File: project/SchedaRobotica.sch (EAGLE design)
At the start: 105 parts, among them IC1 LMZ14202TZE-ADJ_NOPB, IC2 VNH7070ASTR, IC3 VNH7070ASTR, IC4 VNH7070ASTR, IC5 VNH7070ASTR, M1 43650-0201, M2 43650-0201, M3 43650-0201, M4 43650-0201

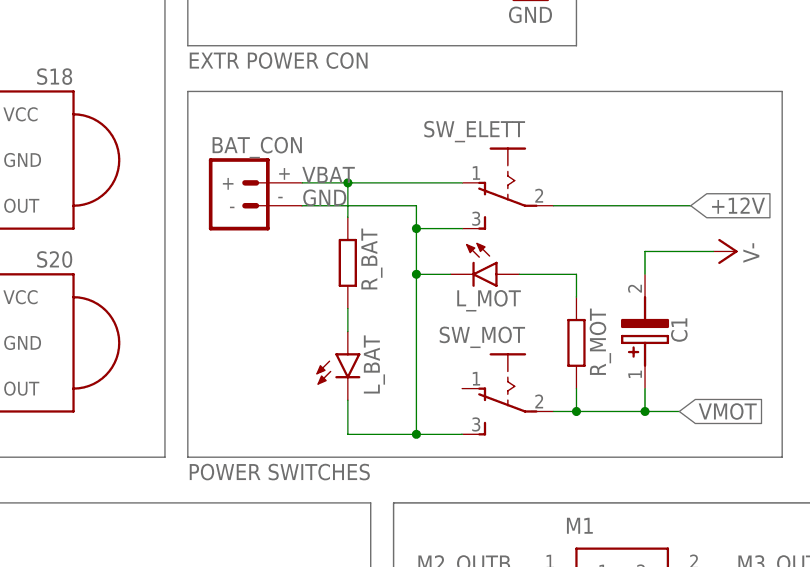
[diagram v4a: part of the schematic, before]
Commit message: started placing components for optimal wiring
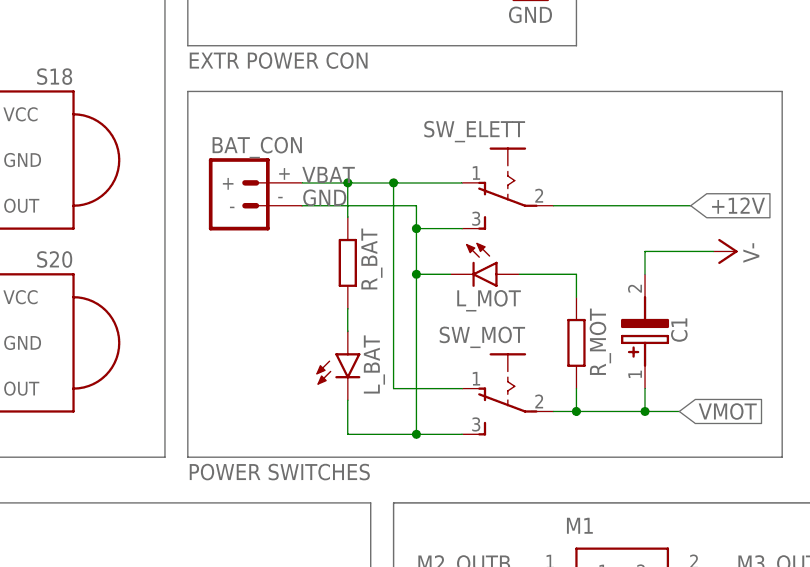
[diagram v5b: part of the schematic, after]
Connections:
- net VBAT: now also SW_MOT.O
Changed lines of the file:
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@@
 <grid distance="0.1" unitdist="inch" unit="inch" style="lines" multiple="1" display="no" altdistance="0.01" altunitdist="inch" altunit="inch"/>
 <layers>
-<layer number="1" name="Top" color="4" fill="1" visible="no" active="no"/>
-<layer number="16" name="Bottom" color="1" fill="1" visible="no" active="no"/>
-<layer number="17" name="Pads" color="2" fill="1" visible="no" active="no"/>
-<layer number="18" name="Vias" color="2" fill="1" visible="no" active="no"/>
-<layer number="19" name="Unrouted" color="6" fill="1" visible="no" active="no"/>
-<layer number="20" name="Dimension" color="24" fill="1" visible="no" active="no"/>
-<layer number="21" name="tPlace" color="7" fill="1" visible="no" active="no"/>
-<layer number="22" name="bPlace" color="7" fill="1" visible="no" active="no"/>
-<layer number="23" name="tOrigins" color="15" fill="1" visible="no" active="no"/>
-<layer number="24" name="bOrigins" color="15" fill="1" visible="no" active="no"/>
-<layer number="25" name="tNames" color="7" fill="1" visible="no" active="no"/>
-<layer number="26" name="bNames" color="7" fill="1" visible="no" active="no"/>
-<layer number="27" name="tValues" color="7" fill="1" visible="no" active="no"/>
-<layer number="28" name="bValues" color="7" fill="1" visible="no" active="no"/>
+<layer number="1" name="Top" color="4" fill="1" visible="yes" active="no"/>
+<layer number="16" name="Bottom" color="1" fill="1" visible="yes" active="no"/>
+<layer number="17" name="Pads" color="2" fill="1" visible="yes" active="no"/>
+<layer number="18" name="Vias" color="2" fill="1" visible="yes" active="no"/>
+<layer number="19" name="Unrouted" color="6" fill="1" visible="yes" active="no"/>
+<layer number="20" name="Dimension" color="24" fill="1" visible="yes" active="no"/>
+<layer number="21" name="tPlace" color="7" fill="1" visible="yes" active="no"/>
+<layer number="22" name="bPlace" color="7" fill="1" visible="yes" active="no"/>
+<layer number="23" name="tOrigins" color="15" fill="1" visible="yes" active="no"/>
+<layer number="24" name="bOrigins" color="15" fill="1" visible="yes" active="no"/>
+<layer number="25" name="tNames" color="7" fill="1" visible="yes" active="no"/>
+<layer number="26" name="bNames" color="7" fill="1" visible="yes" active="no"/>
+<layer number="27" name="tValues" color="7" fill="1" visible="yes" active="no"/>
+<layer number="28" name="bValues" color="7" fill="1" visible="yes" active="no"/>
 <layer number="29" name="tStop" color="7" fill="3" visible="no" active="no"/>
 <layer number="30" name="bStop" color="7" fill="6" visible="no" active="no"/>
@@
 <layer number="35" name="tGlue" color="7" fill="4" visible="no" active="no"/>
 <layer number="36" name="bGlue" color="7" fill="5" visible="no" active="no"/>
-<layer number="37" name="tTest" color="7" fill="1" visible="no" active="no"/>
-<layer number="38" name="bTest" color="7" fill="1" visible="no" active="no"/>
+<layer number="37" name="tTest" color="7" fill="1" visible="yes" active="no"/>
+<layer number="38" name="bTest" color="7" fill="1" visible="yes" active="no"/>
 <layer number="39" name="tKeepout" color="4" fill="11" visible="no" active="no"/>
 <layer number="40" name="bKeepout" color="1" fill="11" visible="no" active="no"/>
@@
 <layer number="44" name="Drills" color="7" fill="1" visible="no" active="no"/>
 <layer number="45" name="Holes" color="7" fill="1" visible="no" active="no"/>
-<layer number="46" name="Milling" color="3" fill="1" visible="no" active="no"/>
-<layer number="47" name="Measures" color="7" fill="1" visible="no" active="no"/>
-<layer number="48" name="Document" color="7" fill="1" visible="no" active="no"/>
-<layer number="49" name="Reference" color="7" fill="1" visible="no" active="no"/>
-<layer number="50" name="dxf" color="7" fill="1" visible="no" active="no"/>
-<layer number="51" name="tDocu" color="7" fill="1" visible="no" active="no"/>
-<layer number="52" name="bDocu" color="7" fill="1" visible="no" active="no"/>
-<layer number="53" name="tGND_GNDA" color="7" fill="9" visible="no" active="no"/>
-<layer number="54" name="bGND_GNDA" color="1" fill="9" visible="no" active="no"/>
-<layer number="56" name="wert" color="7" fill="1" visible="no" active="no"/>
-<layer number="57" name="tCAD" color="7" fill="1" visible="no" active="no"/>
-<layer number="59" name="tCarbon" color="7" fill="1" visible="no" active="no"/>
-<layer number="60" name="bCarbon" color="7" fill="1" visible="no" active="no"/>
-<layer number="61" name="stand" color="7" fill="1" visible="no" active="no"/>
+<layer number="46" name="Milling" color="3" fill="1" visible="yes" active="no"/>
+<layer number="47" name="Measures" color="7" fill="1" visible="yes" active="no"/>
+<layer number="48" name="Document" color="7" fill="1" visible="yes" active="no"/>
+<layer number="49" name="Reference" color="7" fill="1" visible="yes" active="no"/>
+<layer number="50" name="dxf" color="7" fill="1" visible="yes" active="no"/>
+<layer number="51" name="tDocu" color="7" fill="1" visible="yes" active="no"/>
+<layer number="52" name="bDocu" color="7" fill="1" visible="yes" active="no"/>
+<layer number="53" name="tGND_GNDA" color="7" fill="9" visible="yes" active="no"/>
+<layer number="54" name="bGND_GNDA" color="1" fill="9" visible="yes" active="no"/>
+<layer number="56" name="wert" color="7" fill="1" visible="yes" active="no"/>
+<layer number="57" name="tCAD" color="7" fill="1" visible="yes" active="no"/>
+<layer number="59" name="tCarbon" color="7" fill="1" visible="yes" active="no"/>
+<layer number="60" name="bCarbon" color="7" fill="1" visible="yes" active="no"/>
+<layer number="61" name="stand" color="7" fill="1" visible="yes" active="no"/>
 <layer number="88" name="SimResults" color="9" fill="1" visible="yes" active="yes"/>
 <layer number="89" name="SimProbes" color="9" fill="1" visible="yes" active="yes"/>
@@
 <wire x1="248.92" y1="223.52" x2="254" y2="223.52" width="0.1524" layer="91"/>
 <pinref part="R_BAT" gate="G$1" pin="1"/>
-<wire x1="254" y1="223.52" x2="266.7" y2="223.52" width="0.1524" layer="91"/>
+<wire x1="254" y1="223.52" x2="259.08" y2="223.52" width="0.1524" layer="91"/>
+<wire x1="259.08" y1="223.52" x2="266.7" y2="223.52" width="0.1524" layer="91"/>
 <wire x1="254" y1="219.71" x2="254" y2="223.52" width="0.1524" layer="91"/>
 <junction x="254" y="223.52"/>
 <label x="248.92" y="223.52" size="1.778" layer="95"/>
-</segment>
-</net>
+<pinref part="SW_MOT" gate="1" pin="O"/>
+<wire x1="266.7" y1="200.66" x2="259.08" y2="200.66" width="0.1524" layer="91"/>
+<wire x1="259.08" y1="200.66" x2="259.08" y2="223.52" width="0.1524" layer="91"/>
+<junction x="259.08" y="223.52"/>
+</segment>
+</net>

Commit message: added IMU and BT
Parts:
- added BT_CON: 4P-2.0, OPL_Connector:GROVE-CONNECTOR-DIP(4P-2.0)
- added C19, C20: 1u, rcl:C-EUC0805
- added R21, R22: 10k, rcl:R-EU_M0805
- added U$3: (no value), BNO055ada:BNO055
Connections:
- new net IFE: BT_CON.3
- new net N$39: BT_CON.4
- new net SCL: R21.1, U$3.SCL
- new net SDA: R22.1, U$3.SDA
- net +3V3: now also BT_CON.1, C19.1, C20.1, R21.2, R22.2, U$3.3V3
- net GND: now also BT_CON.2, C19.2, C20.2, U$3.GND
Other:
- note added: "BLUETOOTH"
- note added: "IMU"
- note added: "TODO: -add BT serial -add roller and kicker connectors (?)"
- note removed: "TODO: -add BT connector (Grove) -add roller and kicker connectors (?)"

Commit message: added ball switches, what now?
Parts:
- added B_SW_1, B_SW_2: 21810LPSTF, 21810LPSTF:21810LPSTF
- added SV5: (no value), con-lstb:MA12-1
- added SV6: (no value), SparkFun-Connectors:CONN_14LONGPADS
- U$3: value (none) -> BNO055_BNO055; device BNO055ada:BNO055 -> IMU:BNO055_BNO055
- renumbered R4 to R_ELETT
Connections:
- net GND: now also U$1.GND1, U$1.GND2, U$1.GND3, U$1.GND4, U$1.GND5, U$1.GND6
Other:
- note added: "BALL SWITCHES"
- note added: "TODO: -add serials and values -add roller and kicker connectors (?) -add US cons if there's room"
- note removed: "TODO: -add BT serial -add roller and kicker connectors (?)"
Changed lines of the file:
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@@
 <layer number="195" name="mNames" color="7" fill="1" visible="no" active="yes"/>
 <layer number="196" name="mValues" color="7" fill="1" visible="no" active="yes"/>
+<layer number="197" name="ARDUINO_b_PLACE" color="7" fill="1" visible="yes" active="yes"/>
 <layer number="199" name="Contour" color="7" fill="1" visible="no" active="yes"/>
 <layer number="200" name="200bmp" color="1" fill="10" visible="yes" active="yes"/>
@@
 <part name="R2" library="rcl" library_urn="urn:adsk.eagle:library:334" deviceset="R-EU_" device="M0805" package3d_urn="urn:adsk.eagle:package:23556/2"/>
 <part name="R3" library="rcl" library_urn="urn:adsk.eagle:library:334" deviceset="R-EU_" device="M0805" package3d_urn="urn:adsk.eagle:package:23556/2"/>
-<part name="R4" library="rcl" library_urn="urn:adsk.eagle:library:334" deviceset="R-EU_" device="M0805" package3d_urn="urn:adsk.eagle:package:23556/2"/>
+<part name="R_ELETT" library="rcl" library_urn="urn:adsk.eagle:library:334" deviceset="R-EU_" device="M0805" package3d_urn="urn:adsk.eagle:package:23556/2"/>
 <part name="+3V6" library="supply1" library_urn="urn:adsk.eagle:library:371" deviceset="+3V3" device=""/>
 <part name="GND27" library="supply1" library_urn="urn:adsk.eagle:library:371" deviceset="GND" device=""/>
@@
 <part name="M4-" library="led" library_urn="urn:adsk.eagle:library:259" deviceset="LED" device="CHIPLED_1206" package3d_urn="urn:adsk.eagle:package:15823/2"/>
 <part name="M4+" library="led" library_urn="urn:adsk.eagle:library:259" deviceset="LED" device="CHIPLED_1206" package3d_urn="urn:adsk.eagle:package:15823/2"/>
-<part name="U$3" library="BNO055ada" deviceset="BNO055" device=""/>
+<part name="U$3" library="IMU" deviceset="BNO055_BNO055" device=""/>
 <part name="C19" library="rcl" library_urn="urn:adsk.eagle:library:334" deviceset="C-EU" device="C0805" package3d_urn="urn:adsk.eagle:package:23617/2" value="1u"/>
 <part name="R21" library="rcl" library_urn="urn:adsk.eagle:library:334" deviceset="R-EU_" device="M0805" package3d_urn="urn:adsk.eagle:package:23556/2" value="10k"/>
@@
 <part name="+3V14" library="supply1" library_urn="urn:adsk.eagle:library:371" deviceset="+3V3" device=""/>
 <part name="GND39" library="supply1" library_urn="urn:adsk.eagle:library:371" deviceset="GND" device=""/>
+<part name="GND40" library="supply1" library_urn="urn:adsk.eagle:library:371" deviceset="GND" device=""/>
+<part name="SV5" library="con-lstb" library_urn="urn:adsk.eagle:library:162" deviceset="MA12-1" device="" package3d_urn="urn:adsk.eagle:package:8348/1"/>
+<part name="SV6" library="SparkFun-Connectors" deviceset="CONN_14" device="LONGPADS"/>
+<part name="B_SW_1" library="21810LPSTF" deviceset="21810LPSTF" device=""/>
+<part name="B_SW_2" library="21810LPSTF" deviceset="21810LPSTF" device=""/>
 </parts>
 <sheets>
@@
 <text x="259.08" y="142.24" size="1.778" layer="97">MOTOR CONS</text>
 <text x="281.94" y="248.92" size="1.778" layer="91">TODO:
--add BT serial
--add roller and kicker connectors (?)</text>
+-add serials and values
+-add roller and kicker connectors (?)
+-add US cons if there's room</text>
 <text x="340.36" y="101.6" size="2.54" layer="97">M1</text>
 <text x="449.58" y="101.6" size="2.54" layer="97">M2</text>
@@
 <text x="449.58" y="44.45" size="2.54" layer="97">M4</text>
 <wire x1="312.42" y1="187.96" x2="312.42" y2="139.7" width="0.1524" layer="97"/>
-<wire x1="312.42" y1="139.7" x2="363.22" y2="139.7" width="0.1524" layer="97"/>
-<wire x1="363.22" y1="139.7" x2="363.22" y2="187.96" width="0.1524" layer="97"/>
-<wire x1="363.22" y1="187.96" x2="312.42" y2="187.96" width="0.1524" layer="97"/>
+<wire x1="312.42" y1="139.7" x2="365.76" y2="139.7" width="0.1524" layer="97"/>
+<wire x1="365.76" y1="139.7" x2="365.76" y2="187.96" width="0.1524" layer="97"/>
+<wire x1="365.76" y1="187.96" x2="312.42" y2="187.96" width="0.1524" layer="97"/>
 <text x="312.42" y="137.16" size="1.778" layer="97">IMU</text>
 <wire x1="304.8" y1="233.68" x2="304.8" y2="203.2" width="0.1524" layer="97"/>
@@
 <wire x1="332.74" y1="233.68" x2="304.8" y2="233.68" width="0.1524" layer="97"/>
 <text x="304.8" y="200.66" size="1.778" layer="97">BLUETOOTH</text>
+<wire x1="368.3" y1="187.96" x2="368.3" y2="139.7" width="0.1524" layer="97"/>
+<wire x1="368.3" y1="139.7" x2="457.2" y2="139.7" width="0.1524" layer="97"/>
+<wire x1="457.2" y1="139.7" x2="457.2" y2="187.96" width="0.1524" layer="97"/>
+<wire x1="457.2" y1="187.96" x2="368.3" y2="187.96" width="0.1524" layer="97"/>
+<text x="368.3" y="137.16" size="1.778" layer="97">BALL SWITCHES</text>
 </plain>
 <instances>
-<instance part="U$1" gate="G$1" x="45.72" y="50.8" smashed="yes"/>
+<instance part="U$1" gate="G$1" x="40.64" y="55.88" smashed="yes"/>
 <instance part="SV1" gate="1" x="86.36" y="81.28" smashed="yes" rot="R180">
 <attribute name="VALUE" x="87.63" y="99.06" size="1.778" layer="96" rot="R180"/>
@@
 <attribute name="VALUE" x="252.73" y="49.022" size="1.778" layer="96" rot="R180"/>
 </instance>
-<instance part="R4" gate="G$1" x="278.13" y="44.45" smashed="yes" rot="R90">
+<instance part="R_ELETT" gate="G$1" x="278.13" y="44.45" smashed="yes" rot="R90">
 <attribute name="NAME" x="281.7114" y="40.64" size="1.778" layer="95" rot="R90"/>
 <attribute name="VALUE" x="281.432" y="40.64" size="1.778" layer="96" rot="R90"/>
@@
 <attribute name="VALUE" x="417.195" y="14.478" size="1.778" layer="96" rot="R90"/>
 </instance>
-<instance part="U$3" gate="G$1" x="340.36" y="152.4" smashed="yes" rot="R270"/>
+<instance part="U$3" gate="G$1" x="340.36" y="152.4" smashed="yes"/>
 <instance part="C19" gate="G$1" x="332.74" y="172.72" smashed="yes">
 <attribute name="NAME" x="334.264" y="173.101" size="1.778" layer="95"/>
@@
 <instance part="GND39" gate="1" x="325.12" y="208.28" smashed="yes">
 <attribute name="VALUE" x="322.58" y="205.74" size="1.778" layer="96"/>
+</instance>
+<instance part="GND40" gate="1" x="45.72" y="6.35" smashed="yes">
+<attribute name="VALUE" x="43.18" y="3.81" size="1.778" layer="96"/>
+</instance>
+<instance part="SV5" gate="1" x="121.92" y="78.74" smashed="yes">
+<attribute name="VALUE" x="120.65" y="60.96" size="1.778" layer="96"/>
+<attribute name="NAME" x="120.65" y="97.282" size="1.778" layer="95"/>
+</instance>
+<instance part="SV6" gate="G$1" x="182.88" y="55.88" smashed="yes" rot="R180">
+<attribute name="VALUE" x="182.88" y="78.486" size="1.778" layer="96" font="vector" rot="R180"/>
+<attribute name="NAME" x="182.88" y="37.592" size="1.778" layer="95" font="vector" rot="R180"/>
+</instance>
+<instance part="B_SW_1" gate="G$1" x="386.08" y="172.72" smashed="yes">
+<attribute name="NAME" x="392.43" y="177.8" size="1.778" layer="95" align="center-left"/>
+</instance>
+<instance part="B_SW_2" gate="G$1" x="421.64" y="172.72" smashed="yes">
+<attribute name="NAME" x="427.99" y="177.8" size="1.778" layer="95" align="center-left"/>
 </instance>
 </instances>
@@
 <junction x="325.12" y="212.09"/>
 </segment>
+<segment>
+<pinref part="U$1" gate="G$1" pin="GND1"/>
+<wire x1="33.02" y1="12.7" x2="33.02" y2="10.16" width="0.1524" layer="91"/>
+<wire x1="33.02" y1="10.16" x2="35.56" y2="10.16" width="0.1524" layer="91"/>
+<pinref part="U$1" gate="G$1" pin="GND6"/>
+<wire x1="35.56" y1="10.16" x2="38.1" y2="10.16" width="0.1524" layer="91"/>
+<wire x1="38.1" y1="10.16" x2="40.64" y2="10.16" width="0.1524" layer="91"/>
+<wire x1="40.64" y1="10.16" x2="43.18" y2="10.16" width="0.1524" layer="91"/>
+<wire x1="43.18" y1="10.16" x2="45.72" y2="10.16" width="0.1524" layer="91"/>
+<wire x1="45.72" y1="10.16" x2="45.72" y2="12.7" width="0.1524" layer="91"/>
+<pinref part="U$1" gate="G$1" pin="GND2"/>
+<wire x1="35.56" y1="12.7" x2="35.56" y2="10.16" width="0.1524" layer="91"/>
+<junction x="35.56" y="10.16"/>
+<pinref part="U$1" gate="G$1" pin="GND3"/>
+<wire x1="38.1" y1="12.7" x2="38.1" y2="10.16" width="0.1524" layer="91"/>
+<junction x="38.1" y="10.16"/>
+<pinref part="U$1" gate="G$1" pin="GND4"/>
+<wire x1="40.64" y1="12.7" x2="40.64" y2="10.16" width="0.1524" layer="91"/>
+<junction x="40.64" y="10.16"/>
+<pinref part="U$1" gate="G$1" pin="GND5"/>
+<wire x1="43.18" y1="12.7" x2="43.18" y2="10.16" width="0.1524" layer="91"/>
+<junction x="43.18" y="10.16"/>
+<wire x1="45.72" y1="10.16" x2="45.72" y2="8.89" width="0.1524" layer="91"/>
+<junction x="45.72" y="10.16"/>
+<pinref part="GND40" gate="1" pin="GND"/>
+</segment>
 </net>
 <net name="+3V3" class="0">
@@
 <wire x1="242.57" y1="55.88" x2="278.13" y2="55.88" width="0.1524" layer="91"/>
 <wire x1="278.13" y1="55.88" x2="278.13" y2="49.53" width="0.1524" layer="91"/>
-<pinref part="R4" gate="G$1" pin="2"/>
+<pinref part="R_ELETT" gate="G$1" pin="2"/>
 </segment>
 </net>
@@
 <segment>
 <pinref part="L_ELETT" gate="G$1" pin="A"/>
-<pinref part="R4" gate="G$1" pin="1"/>
+<pinref part="R_ELETT" gate="G$1" pin="1"/>
 <wire x1="278.13" y1="36.83" x2="278.13" y2="39.37" width="0.1524" layer="91"/>
 </segment>

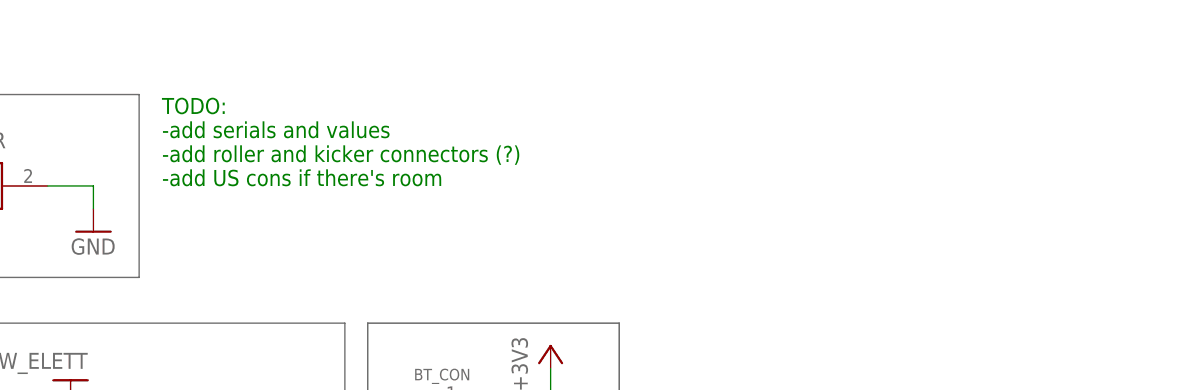
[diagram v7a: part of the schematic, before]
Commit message: rotated ball sensors, what now?
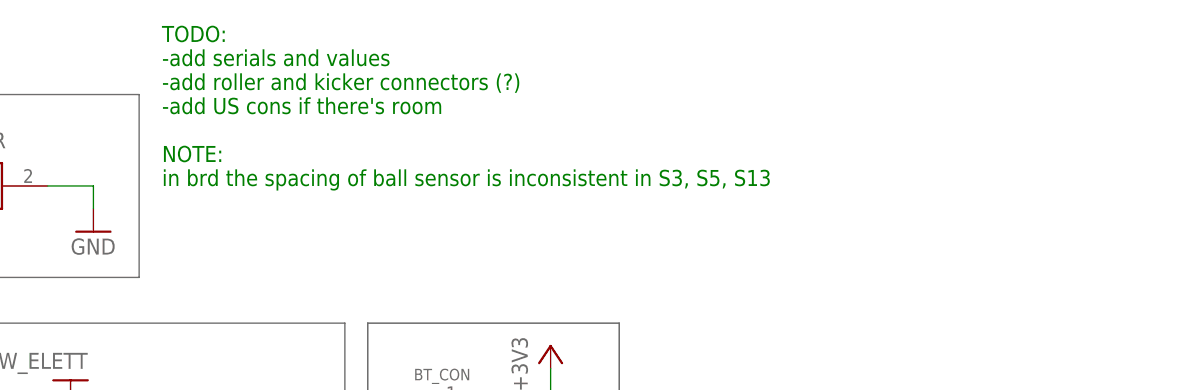
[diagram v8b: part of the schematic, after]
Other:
- note added: "TODO: -add serials and values -add roller and kicker connectors (?) -add US cons if there's room NOTE: in brd the spacing of ball sensor is inconsistent in S3, S5, S13"
- note removed: "TODO: -add serials and values -add roller and kicker connectors (?) -add US cons if there's room"
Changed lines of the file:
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@@
 -add serials and values
 -add roller and kicker connectors (?)
--add US cons if there's room</text>
+-add US cons if there's room
+NOTE:
+in brd the spacing of ball sensor is inconsistent in S3, S5, S13</text>
 <text x="340.36" y="101.6" size="2.54" layer="97">M1</text>
 <text x="449.58" y="101.6" size="2.54" layer="97">M2</text>
